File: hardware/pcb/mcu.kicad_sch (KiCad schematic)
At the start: 1 part, among them U1 SF32LB52xUx

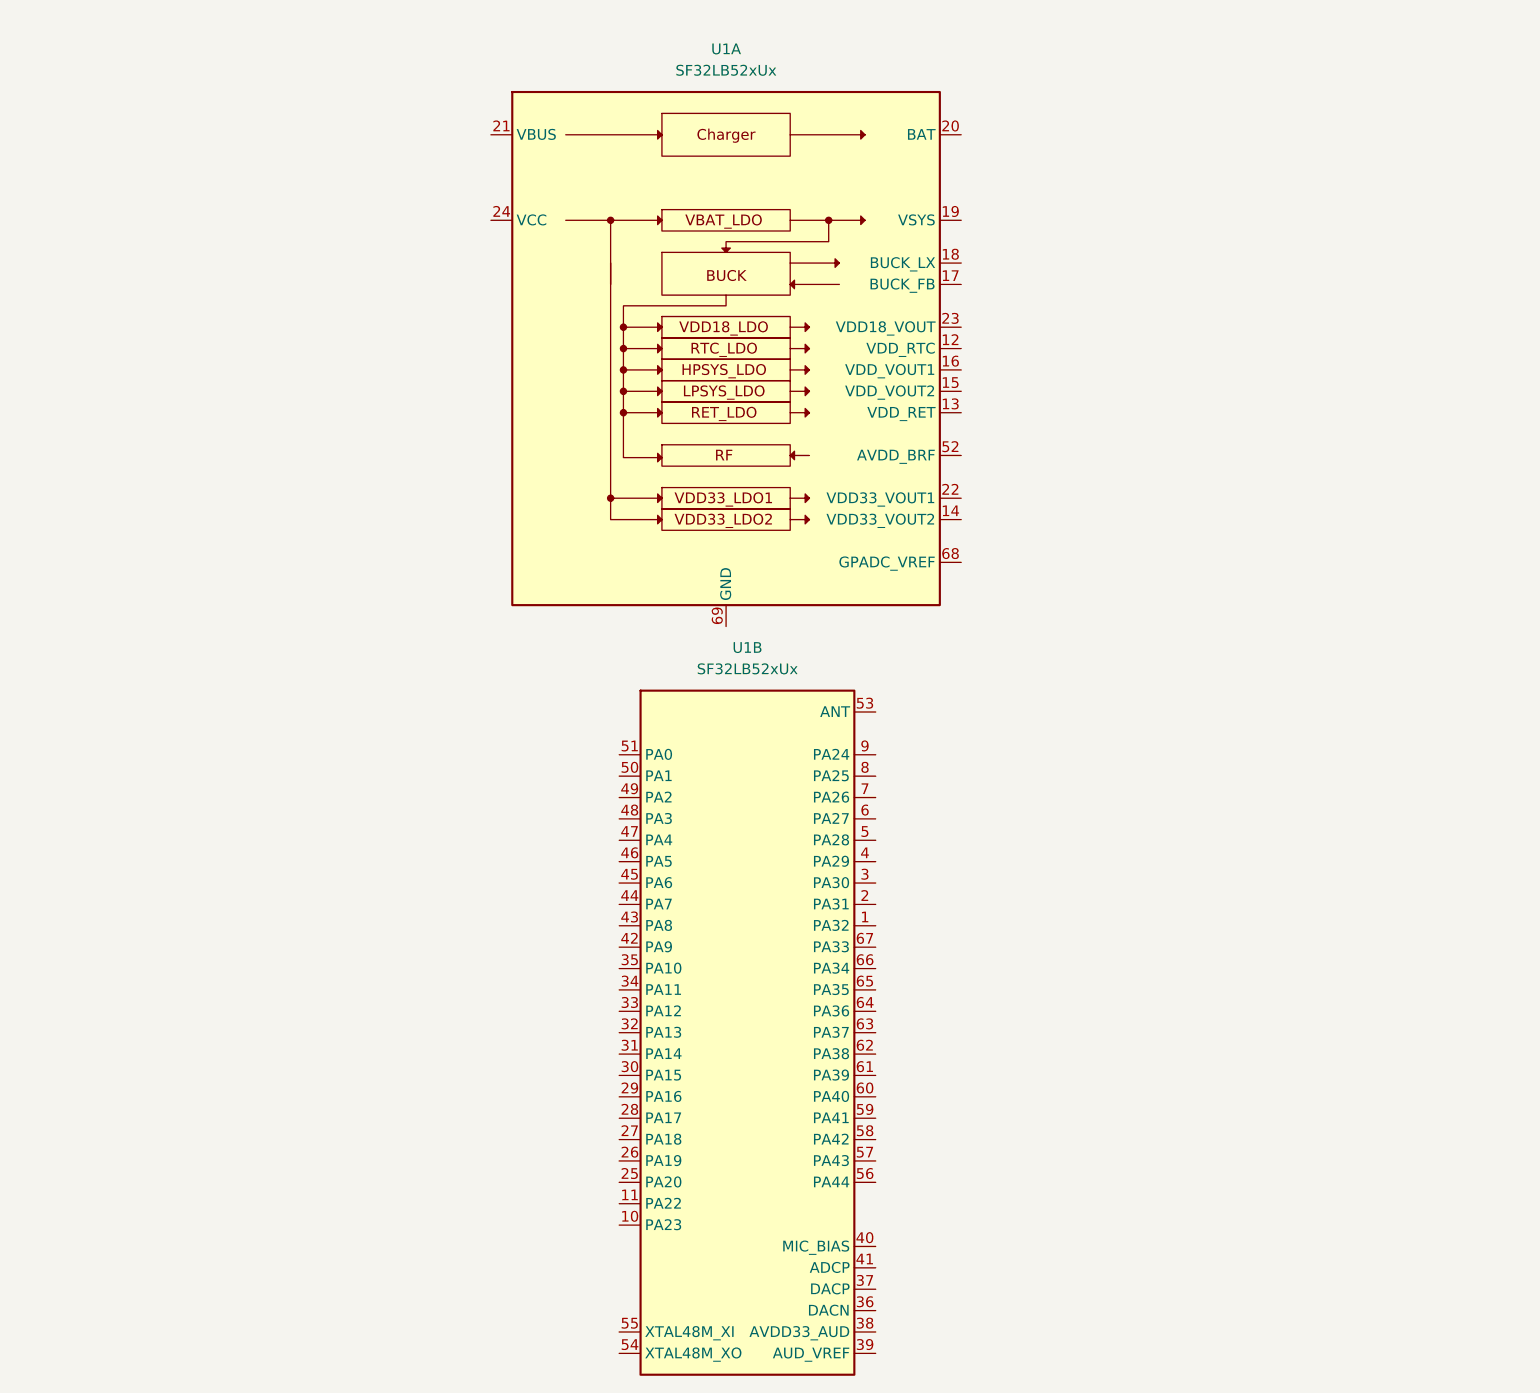
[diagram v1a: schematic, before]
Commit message: Added USB-C to UART connectivity for debugging and flashing
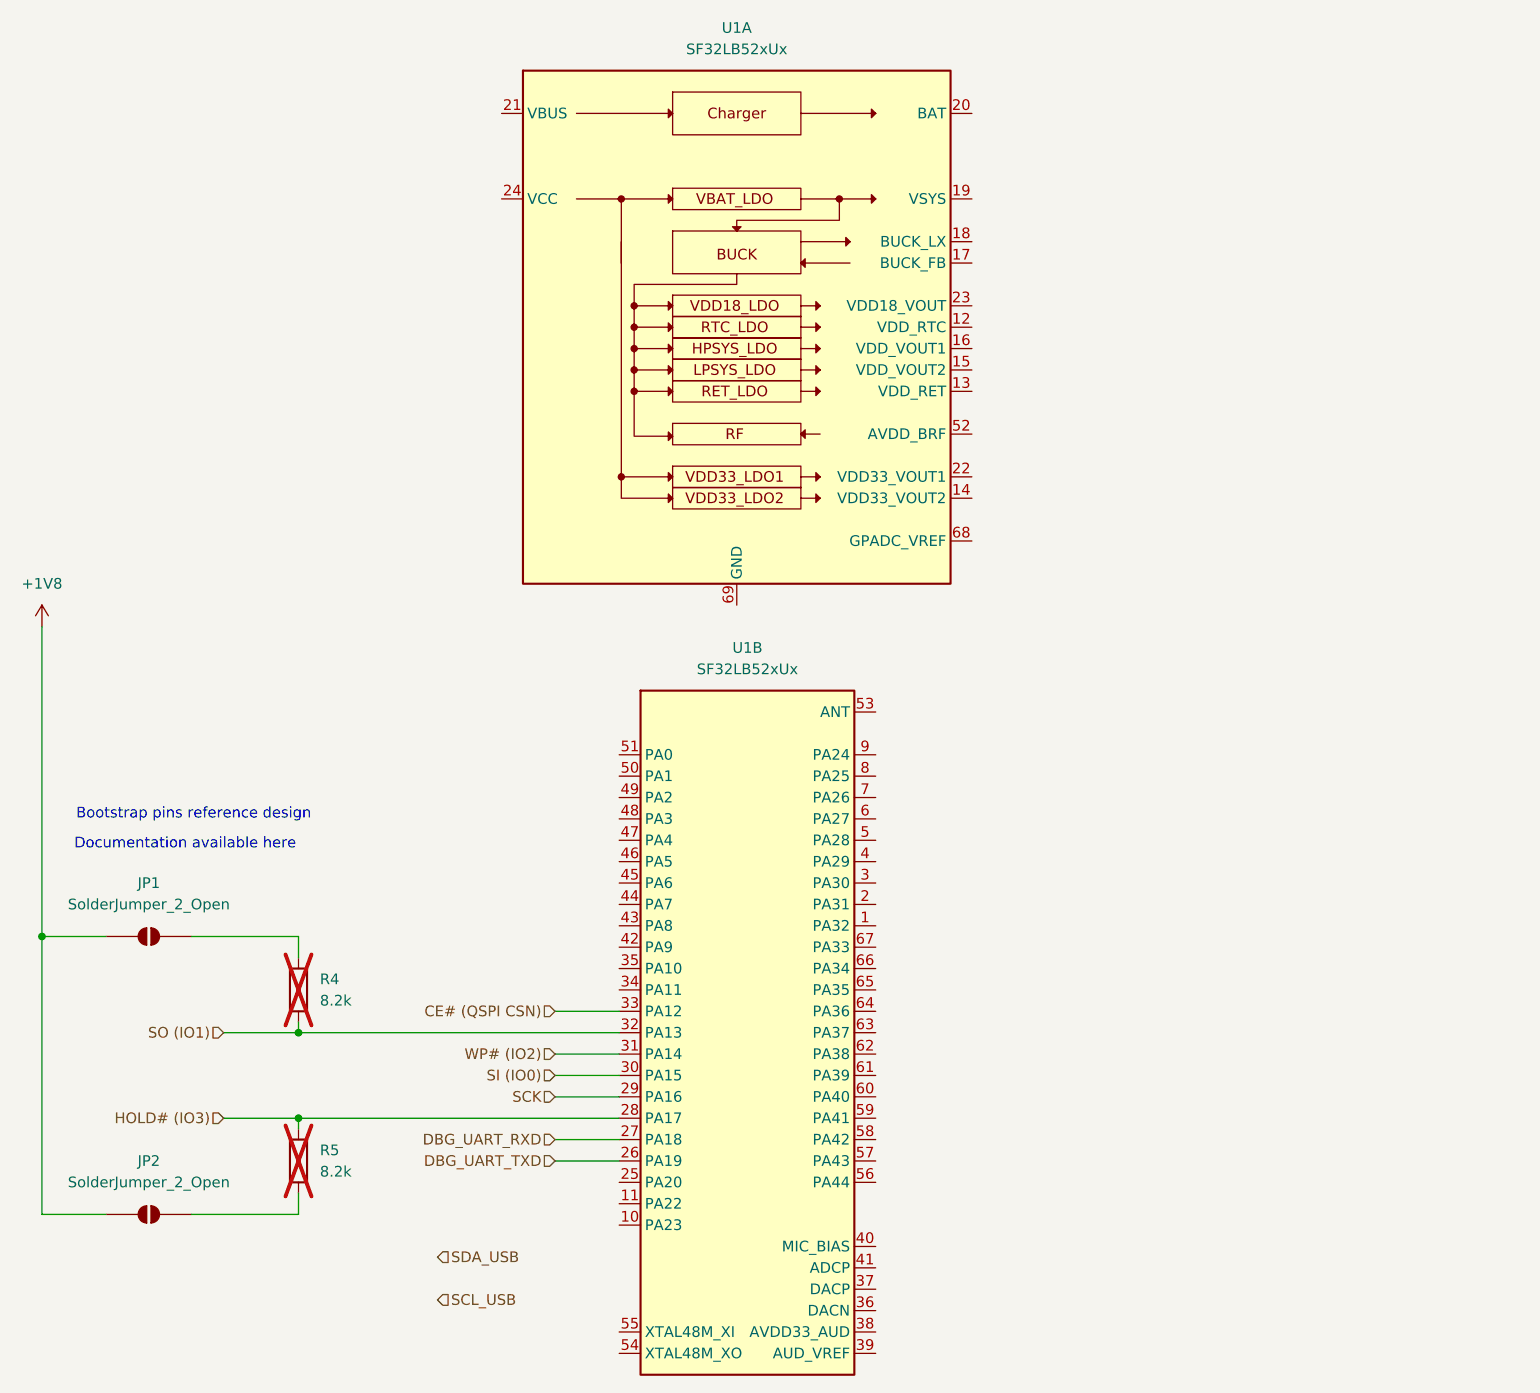
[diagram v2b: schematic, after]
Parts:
- added JP1, JP2: SolderJumper_2_Open, symbol Jumper:SolderJumper_2_Open
- added R4, R5: 8.2k_0402, PCM_4ms_Resistor:R_0402, symbol PCM_4ms_Resistor:8.2k_0402
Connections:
- net DBG_UART_TXD: now reaches U1.26 (PA19)
- net DBG_UART_RXD: now reaches U1.27 (PA18)
- net HOLD# (IO3): now reaches U1.28 (PA17)
- net HOLD# (IO3): now also R5.1
- net SCK: now reaches U1.29 (PA16)
- net SI (IO0): now reaches U1.30 (PA15)
- net WP# (IO2): now reaches U1.31 (PA14)
- net SO (IO1): now reaches U1.32 (PA13)
- net SO (IO1): now also R4.2
- net CE# (QSPI CSN): now reaches U1.33 (PA12)
- new net: JP1.2 (B), R4.1
- new net: JP2.2 (B), R5.2
- new net +1V8: JP1.1 (A), JP2.1 (A)
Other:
- note added: "Bootstrap pins reference design"
- note added: "Documentation available here"
- moved on the sheet: U1A

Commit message: Fixing 3V3 - 1V8 mismatch.
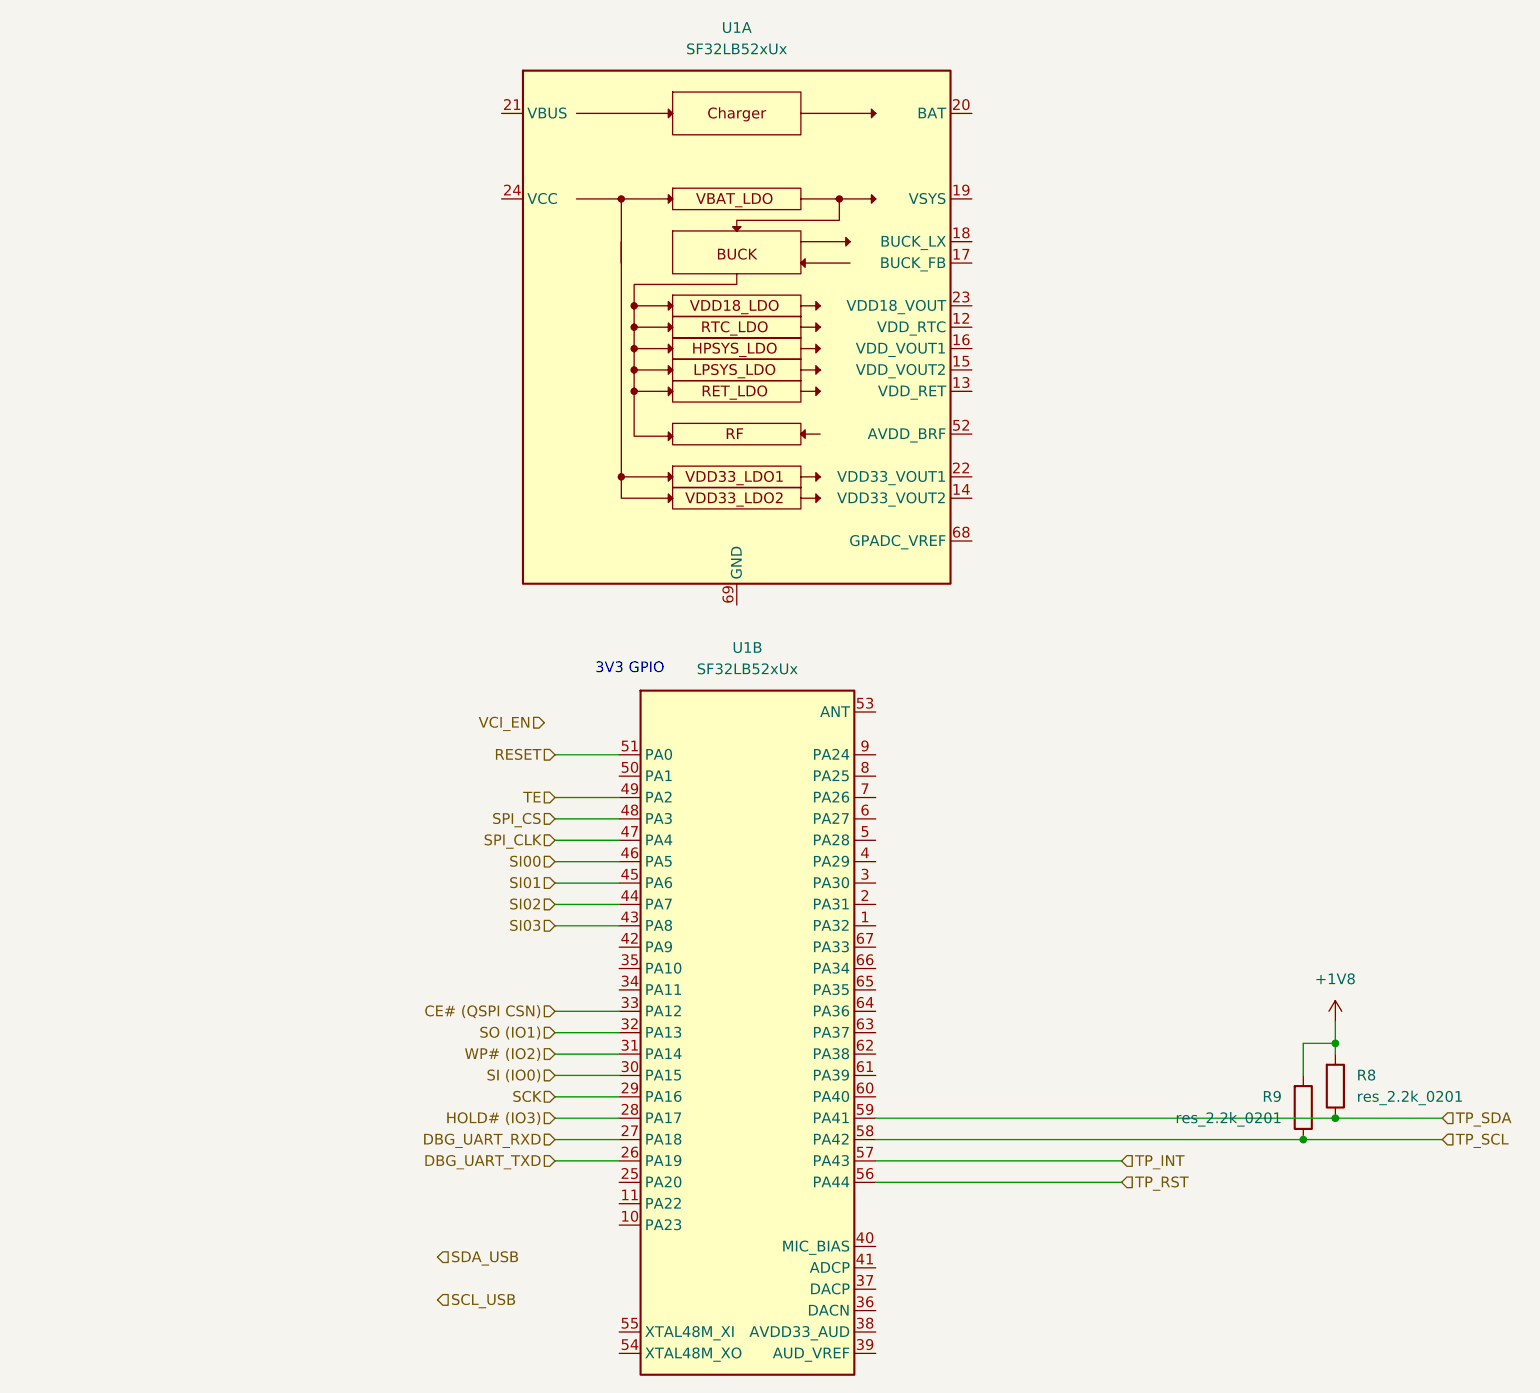
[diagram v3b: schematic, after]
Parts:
- removed JP1, JP2: SolderJumper_2_Open, symbol Jumper:SolderJumper_2_Open
- removed R4, R5: 8.2k_0402, PCM_4ms_Resistor:R_0402, symbol PCM_4ms_Resistor:8.2k_0402
- added R8, R9: res_2.2k_0201, PCM_Resistor_SMD_AKL:R_0201_0603Metric, symbol symbols:res_2.2k_0201
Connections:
- net +1V8: now also R8.1, R9.1
- net SI03: now reaches U1.43 (PA8)
- net SI02: now reaches U1.44 (PA7)
- net SI01: now reaches U1.45 (PA6)
- net SI00: now reaches U1.46 (PA5)
- net SPI_CLK: now reaches U1.47 (PA4)
- net SPI_CS: now reaches U1.48 (PA3)
- net TE: now reaches U1.49 (PA2)
- net RESET: now reaches U1.51 (PA0)
- net TP_RST: now reaches U1.56 (PA44)
- net TP_INT: now reaches U1.57 (PA43)
- net TP_SCL: now reaches U1.58 (PA42)
- net TP_SCL: now also R9.2
- net TP_SDA: now reaches U1.59 (PA41)
- net TP_SDA: now also R8.2
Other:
- note added: "3V3 GPIO"
- note removed: "Bootstrap pins reference design"
- note removed: "Documentation available here"

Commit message: Progress on 3V3 circuit versions.
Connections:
- net SPEAKER_N: now reaches U1.36 (DACN)
- net SPEAKER_P: now reaches U1.37 (DACP)
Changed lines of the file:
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@@
+	)
+	(junction
+		(at 139.7 148.59)
+		(diameter 0)
+		(color 0 0 0 0)
 	)
 	(junction
@@
 	)
 	(junction
+		(at 139.7 151.13)
+		(diameter 0)
+		(color 0 0 0 0)
+	)
+	(junction
 		(at 194.31 143.51)
 		(diameter 0)
@@
 	(wire
 		(pts
+			(xy 139.7 163.83) (xy 149.86 163.83)
+		)
+		(stroke
+			(width 0)
+			(type default)
+		)
+	)
+	(wire
+		(pts
 			(xy 194.31 134.62) (xy 194.31 135.89)
 		)
@@
 	(wire
 		(pts
+			(xy 128.27 148.59) (xy 139.7 148.59)
+		)
+		(stroke
+			(width 0)
+			(type default)
+		)
+	)
+	(wire
+		(pts
 			(xy 101.6 140.97) (xy 109.22 140.97)
 		)
@@
 	(wire
 		(pts
+			(xy 139.7 148.59) (xy 149.86 148.59)
+		)
+		(stroke
+			(width 0)
+			(type default)
+		)
+	)
+	(wire
+		(pts
 			(xy 101.6 107.95) (xy 109.22 107.95)
 		)
@@
 	(wire
 		(pts
+			(xy 139.7 151.13) (xy 149.86 151.13)
+		)
+		(stroke
+			(width 0)
+			(type default)
+		)
+	)
+	(wire
+		(pts
 			(xy 101.6 130.81) (xy 109.22 130.81)
 		)
@@
 	(wire
 		(pts
+			(xy 139.7 166.37) (xy 149.86 166.37)
+		)
+		(stroke
+			(width 0)
+			(type default)
+		)
+	)
+	(wire
+		(pts
 			(xy 101.6 135.89) (xy 109.22 135.89)
 		)
@@
 	(wire
 		(pts
-			(xy 139.7 148.59) (xy 168.91 148.59)
-		)
-		(stroke
-			(width 0)
-			(type default)
-		)
-	)
-	(wire
-		(pts
-			(xy 139.7 151.13) (xy 168.91 151.13)
-		)
-		(stroke
-			(width 0)
-			(type default)
-		)
-	)
-	(wire
-		(pts
 			(xy 190.5 134.62) (xy 194.31 134.62)
 		)
@@
 	(wire
 		(pts
+			(xy 128.27 151.13) (xy 139.7 151.13)
+		)
+		(stroke
+			(width 0)
+			(type default)
+		)
+	)
+	(wire
+		(pts
 			(xy 101.6 118.11) (xy 109.22 118.11)
 		)
@@
 		)
 	)
+	(hierarchical_label "GNSS_RXD"
+		(shape input)
+		(at 153.67 102.87 0)
+		(effects
+			(font
+				(size 1.27 1.27)
+			)
+			(justify left)
+		)
+	)
+	(hierarchical_label "SPEAKER_N"
+		(shape input)
+		(at 149.86 166.37 0)
+		(effects
+			(font
+				(size 1.27 1.27)
+			)
+			(justify left)
+		)
+	)
 	(hierarchical_label "SPI_CLK"
 		(shape input)
@@
 	(hierarchical_label "SDA_USB"
 		(shape input)
-		(at 87.63 160.02 0)
+		(at 153.67 116.84 0)
+		(effects
+			(font
+				(size 1.27 1.27)
+			)
+			(justify left)
+		)
+	)
+	(hierarchical_label "GNSS_RESET"
+		(shape input)
+		(at 153.67 110.49 0)
 		(effects
 			(font
@@
 		)
 	)
+	(hierarchical_label "GNSS_EN"
+		(shape input)
+		(at 153.67 107.95 0)
+		(effects
+			(font
+				(size 1.27 1.27)
+			)
+			(justify left)
+		)
+	)
 	(hierarchical_label "SI (IO0)"
 		(shape input)
@@
 		)
 	)
+	(hierarchical_label "GNSS_TXD"
+		(shape input)
+		(at 153.67 100.33 0)
+		(effects
+			(font
+				(size 1.27 1.27)
+			)
+			(justify left)
+		)
+	)
 	(hierarchical_label "VCI_EN"
 		(shape input)
@@
 	(hierarchical_label "TP_RST"
 		(shape input)
-		(at 168.91 151.13 0)
+		(at 149.86 151.13 0)
 		(effects
 			(font
@@
 		)
 	)
+	(hierarchical_label "GNSS_TIMEPULSE"
+		(shape input)
+		(at 153.67 105.41 0)
+		(effects
+			(font
+				(size 1.27 1.27)
+			)
+			(justify left)
+		)
+	)
+	(hierarchical_label "SPEAKER_P"
+		(shape input)
+		(at 149.86 163.83 0)
+		(effects
+			(font
+				(size 1.27 1.27)
+			)
+			(justify left)
+		)
+	)
 	(hierarchical_label "SCK"
 		(shape input)
@@
 	(hierarchical_label "SCL_USB"
 		(shape input)
-		(at 87.63 165.1 0)
+		(at 153.67 119.38 0)
 		(effects
 			(font
@@
 		)
 	)
+	(hierarchical_label "GNSS_EXTINT"
+		(shape input)
+		(at 153.67 113.03 0)
+		(effects
+			(font
+				(size 1.27 1.27)
+			)
+			(justify left)
+		)
+	)
 	(hierarchical_label "SI03"
 		(shape input)
@@
 	(hierarchical_label "TP_INT"
 		(shape input)
-		(at 168.91 148.59 0)
-		(effects
-			(font
+		(at 149.86 148.59 0)
+		(effects
+			(font

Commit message: Updated broken flash schematic.
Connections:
- net CE# (QSPI CSN) renamed FLASH CS#
- net HOLD# (IO3) renamed FLASH IO3
- net SCK renamed FLASH SCK
- net SI (IO0) renamed FLASH IO0
- net SO (IO1) renamed FLASH IO1
- net WP# (IO2) renamed FLASH IO2
